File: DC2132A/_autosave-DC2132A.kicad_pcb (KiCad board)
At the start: 2 copper layers, 10 parts, among them U3 LT8612, U4 LT3092

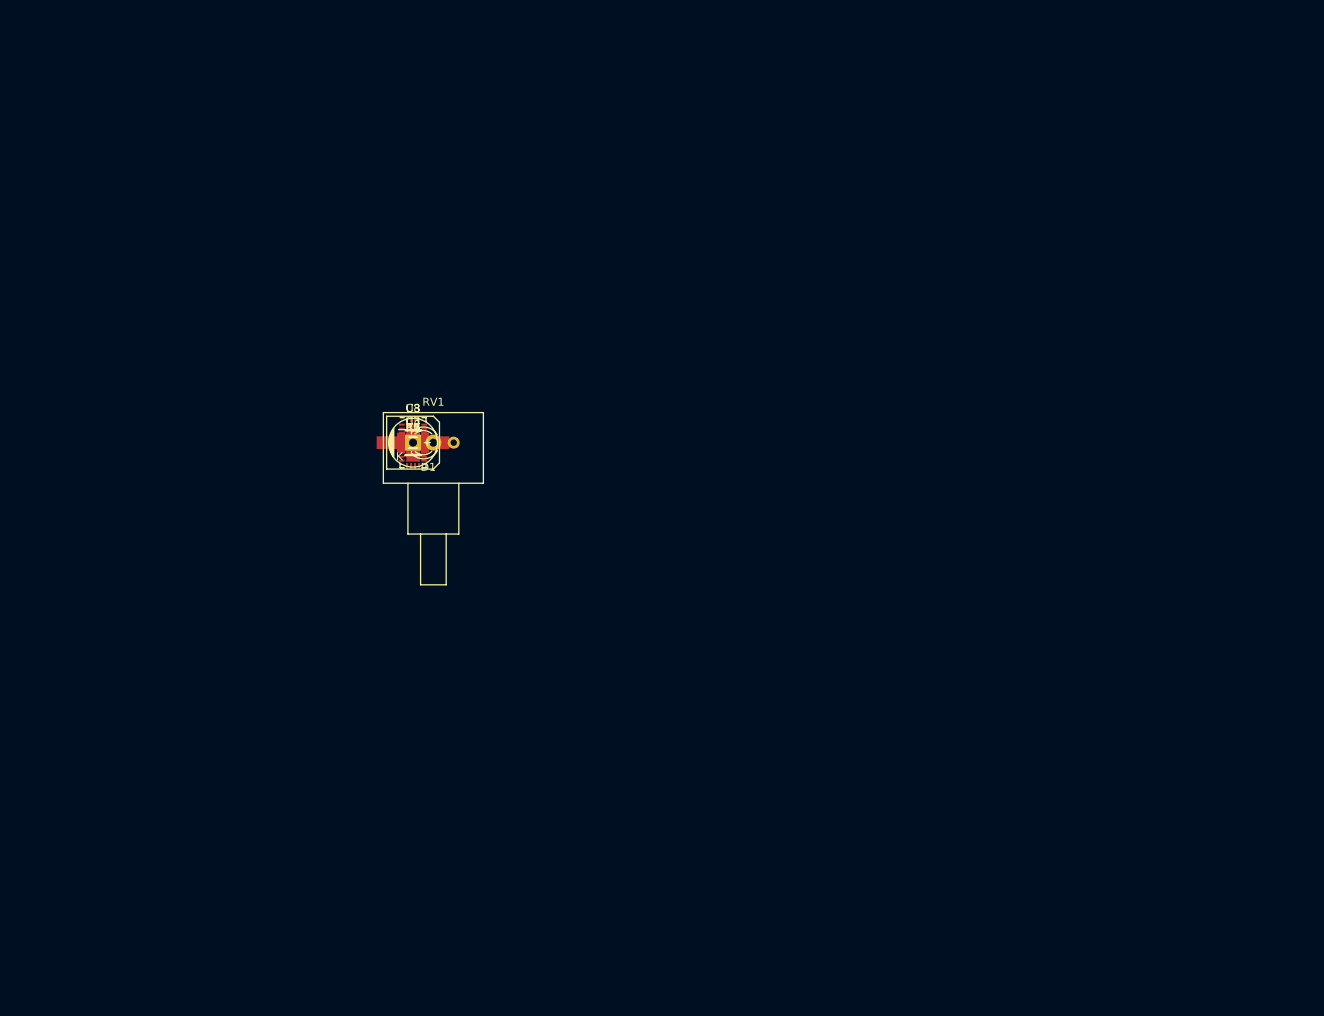
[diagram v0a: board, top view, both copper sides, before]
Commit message: added more components from lt schematic
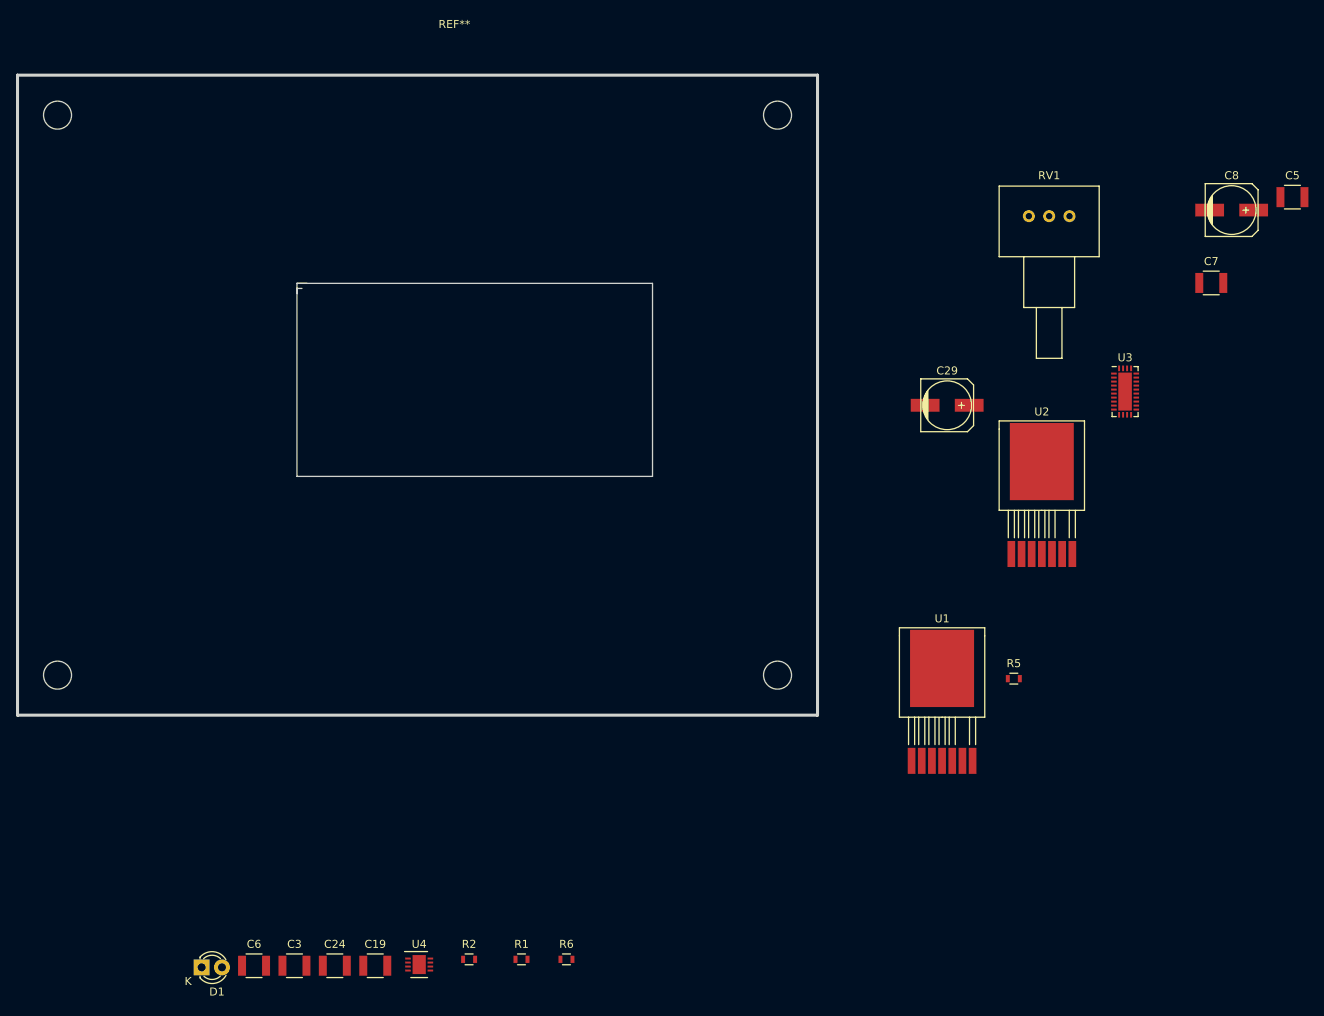
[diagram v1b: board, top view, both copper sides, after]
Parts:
- added C19: 10uF, Capacitors_SMD:C_1210, F.Cu at (143.8, 170.4)
- added C24: 10uF, Capacitors_SMD:C_1210, F.Cu at (138.7, 170.4)
- added C29: 100uF, Capacitors_SMD:c_elec_6.3x7.7, F.Cu at (215.3, 100.3)
- added C5: 10uF, Capacitors_SMD:C_1210, F.Cu at (258.4, 74.3)
- added C6: 10uF, Capacitors_SMD:C_1210, F.Cu at (128.6, 170.4)
- added C7: 10uF, Capacitors_SMD:C_1210, F.Cu at (248.3, 85.0)
- added REF**: EuroBoard_halb_Type-I_100mmX80mm_holes, EuroBoard_Outline:EuroBoard_halb_Type-I_100mmX80mm_holes, F.Cu at (99.1, 139.1)
- added U1: LT3081, DC2132A:TO-263-8, F.Cu at (214.6, 144.8)
- added U2: LT3081, DC2132A:TO-263-8, F.Cu at (227.1, 118.9)
- moved C8 106.4 mm to (250.8, 75.9)
- moved U3 89.2 mm to (237.5, 98.6)
- moved RV1 82.0 mm to (225.5, 76.7)
- moved R5 80.7 mm to (223.6, 134.5)
- moved D1 70.7 mm to (122.1, 170.6)
- moved R6 67.4 mm to (167.7, 169.6)
- moved C3 67.0 mm to (133.7, 170.4)
- moved R1 66.0 mm to (162.1, 169.6)
- moved U4 65.2 mm to (149.3, 170.2)
- moved R2 65.0 mm to (155.5, 169.6)
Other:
- board outline added: 100 x 80 mm
